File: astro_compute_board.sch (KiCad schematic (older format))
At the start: 76 parts, among them J1 SWD, J2 Conn_01x04, J3 Conn_01x04, J4 Heater01, J5 GPIO_CONNECTOR, J6 USB_B_Micro, J7 Heater01, J8 RaspberryHeader, Q1 QM6015D, Q2 IRF540S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

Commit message: Board almost done. Major simplifications ahead
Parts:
- added H1, H2, H3, H4: MountingHole_Pad, MountingHole:MountingHole_3.2mm_M3_Pad_Via, symbol Mechanical:MountingHole_Pad
- added J10: ADC_IO, Connector_Molex:Molex_PicoBlade_53048-0510_1x05_P1.25mm_Horizontal, symbol Connector_Generic:Conn_01x05
- C1, C2: footprint (none) -> Capacitor_SMD:C_0603_1608Metric
- C10, C11, C12, C3, C4, C5, C6, C7, C8, C9: footprint (none) -> Capacitor_SMD:C_0402_1005Metric
- C13, C14, C15, C16, C17, C18: footprint (none) -> Capacitor_SMD:C_1206_3216Metric
- C19, C20, C21, C22, C23, C24: renamed from C?; footprint (none) -> Capacitor_SMD:C_1206_3216Metric
- D1: footprint (none) -> LED_SMD:LED_0603_1608Metric
- F1: footprint (none) -> Fuse:Fuse_1206_3216Metric
- FB1: footprint (none) -> Inductor_SMD:L_0805_2012Metric
- GPIO1: renamed from J5; footprint (none) -> Connector_PinHeader_1.27mm:PinHeader_2x05_P1.27mm_Vertical_SMD
- J1: footprint (none) -> Connector_PinHeader_1.27mm:PinHeader_2x05_P1.27mm_Vertical_SMD
- J2: value Conn_01x04 -> I2C1; footprint (none) -> Connector_Molex:Molex_PicoBlade_53048-0410_1x04_P1.25mm_Horizontal
- J6: footprint (none) -> Connector_USB:USB_Micro-AB_Molex_47590-0001
- J8: footprint (none) -> Connector_PinHeader_2.54mm:PinHeader_2x20_P2.54mm_Vertical
- J9: renamed from J?; value Heater01 -> VINPUT
- L1: footprint (none) -> Inductor_SMD:L_0402_1005Metric
- L2: footprint (none) -> Inductor_SMD:L_Sunlord_MWSA0518_5.4x5.2mm
- L3: renamed from L?; footprint (none) -> Inductor_SMD:L_Sunlord_MWSA0518_5.4x5.2mm
- R1, R12, R13, R14, R15, R16, R17, R2: footprint (none) -> Resistor_SMD:R_0402_1005Metric
- R10, R11, R18, R19, R3, R6, R7, R8, R9: footprint (none) -> Resistor_SMD:R_0603_1608Metric
- R20, R21: renamed from R?; footprint (none) -> Resistor_SMD:R_0805_2012Metric
- R22, R23, R24, R25: renamed from R?; footprint (none) -> Resistor_SMD:R_0603_1608Metric
- R4, R5: footprint (none) -> Resistor_SMD:R_0805_2012Metric
- SW1: footprint (none) -> Button_Switch_SMD:SW_SPDT_PCM12
- U2: footprint (none) -> Package_SO:SOIC-8-1EP_3.9x4.9mm_P1.27mm_EP2.29x3mm
- U4: renamed from U?; footprint (none) -> Package_SO:SOIC-8-1EP_3.9x4.9mm_P1.27mm_EP2.29x3mm
- USART1: renamed from J3; footprint (none) -> Connector_Molex:Molex_PicoBlade_53048-0410_1x04_P1.25mm_Horizontal
- Y1: footprint (none) -> Crystal:Crystal_SMD_3225-4Pin_3.2x2.5mm
- gave numbers to parts that had none: 1
- renumbered J4 to Heater1, J7 to Heater2
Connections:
- wire segments 254 -> 263
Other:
- moved on the sheet: C19, C20, C21, C22, C23, C24, J9, L3, R22, R23, R24, R25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

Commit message: JLCPCB Ready (but costly)
Contains many extender parts that make PCB expensive.
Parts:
- removed C21: Open, Capacitor_SMD:C_1206_3216Metric, symbol Device:C_Small
- removed C22: 0.1u, Capacitor_SMD:C_1206_3216Metric, symbol Device:C_Small
- removed C23: 2.2nF, Capacitor_SMD:C_1206_3216Metric, symbol Device:C_Small
- removed C24: 22uF, Capacitor_SMD:C_1206_3216Metric, symbol Device:C_Small
- removed J2: I2C1, Connector_Molex:Molex_PicoBlade_53048-0410_1x04_P1.25mm_Horizontal, symbol Connector_Generic:Conn_01x04
- removed L3: 6.8uH, Inductor_SMD:L_Sunlord_MWSA0518_5.4x5.2mm, symbol Device:L_Small
- removed R25: 24k, Resistor_SMD:R_0603_1608Metric, symbol Device:R_Small
- removed TP1, TP2: TestPoint, TestPoint:TestPoint_Pad_D2.0mm, symbol Connector:TestPoint
- removed U4: RT7257BHZSP, Package_SO:SOIC-8-1EP_3.9x4.9mm_P1.27mm_EP2.29x3mm, symbol project_custom_symbols:RT7257BHZSP
- added D2: B5817W-5819W, Diode_SMD:D_SOD-123, symbol Device:D_Schottky_Small
- added D3, D4: RED, LED_SMD:LED_0603_1608Metric, symbol Device:LED_Small
- added D5: Green, LED_SMD:LED_0603_1608Metric, symbol Device:LED_Small
- added U4: LM1117-3.3, Package_TO_SOT_SMD:SOT-223, symbol Regulator_Linear:LM1117-3.3
- C1, C2: LCSC Part # (none) -> C23630
- C10: LCSC Part # (none) -> C15195
- C11, C12: LCSC Part # (none) -> C1547
- C13, C19, C20: LCSC Part # (none) -> C13585
- C14, C16: LCSC Part # (none) -> C24497
- C15: value Open -> 22uF; LCSC Part # (none) -> C5672
- C17: LCSC Part # (none) -> C35220
- C18: LCSC Part # (none) -> C5672
- C3: value 4uF -> 4.7uF; LCSC Part # (none) -> C23733
- C4, C5, C6, C7, C8: LCSC Part # (none) -> C1525
- C9: LCSC Part # (none) -> C52923
- D1: value LED_Small -> BLUE; LCSC Part # (none) -> C72041
- F1: LCSC Part # (none) -> C315895
- FB1: LCSC Part # (none) -> C1017
- L1: LCSC Part # (none) -> C26443
- L2: LCSC Part # (none) -> C408348
- Q1: LCSC Part # (none) -> C238708
- Q2, Q3: LCSC Part # (none) -> C725068
- R1: LCSC Part # (none) -> C25744
- R10, R18: LCSC Part # (none) -> C21190
- R11, R19: LCSC Part # (none) -> C22961
- R12, R13, R14, R15, R16, R17: LCSC Part # (none) -> C25092
- R2: LCSC Part # (none) -> C25118
- R20, R21, R4, R5: LCSC Part # (none) -> C17520
- R22: value 100k -> 1k; LCSC Part # (none) -> C21190
- R23: value 22k -> 1k; LCSC Part # (none) -> C21190
- R24: value 75k -> 1k; LCSC Part # (none) -> C21190
- R3: value 10k -> 2k; LCSC Part # (none) -> C22975
- R6: LCSC Part # (none) -> C25803
- R7: value 22k -> 33k; LCSC Part # (none) -> C4216
- R8: value 75k -> 62k; LCSC Part # (none) -> C23221
- R9: value 24k -> 11.8k; LCSC Part # (none) -> C22861
- U1: LCSC Part # (none) -> C15742
- U2: LCSC Part # (none) -> C27998
- U3: LCSC Part # (none) -> C7519
- U5: LCSC Part # (none) -> C94847
- Y1: LCSC Part # (none) -> C13738
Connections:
- net labels removed: PWM_A1, PWM_B1
- wire segments 263 -> 238
- no-connect marks 50 -> 53
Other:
- moved on the sheet: C13, C14, C16, C17, C18, H1, H2, H3, H4, Heater1, Heater2, J9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

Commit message: Rev2 - Out of Stock componets update (JLCPCB)
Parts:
- added R25: 800, Resistor_SMD:R_0603_1608Metric, symbol Device:R_Small
- C15, C18: footprint Capacitor_SMD:C_1206_3216Metric -> Capacitor_SMD:C_0805_2012Metric; LCSC Part # C5672 -> C45783
- C17: footprint Capacitor_SMD:C_1206_3216Metric -> Capacitor_SMD:C_0805_2012Metric; LCSC Part # C35220 -> C28260
- D2: LCSC Part # C84032 -> C8598
- F1: LCSC Part # C315895 -> (none)
- J6: footprint Connector_USB:USB_Micro-AB_Molex_47590-0001 -> Connector_USB:USB_Micro-B_Molex-105017-0001; LCSC Part # (none) -> C404969
- Q2, Q3: symbol IRF540:IRF540 -> astro_compute_board-rescue:IRF540-IRF540
- R9: value 11.8k -> 11k; LCSC Part # C22861 -> C25950
- SW1: LCSC Part # (none) -> C431541
- U1: value STM32F405RGTx -> STM32F103R8T6; LCSC Part # C15742 -> C46034
- U2: LCSC Part # C27998 -> C130799
- U5: LCSC Part # C94847 -> C129490
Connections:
- net +3V3: no longer J8.1 (Pin_1), J8.17 (Pin_17)
- net GND: now also R25.1; no longer R9.1
- new net: R25.2, R9.1
- no-connect marks 53 -> 55
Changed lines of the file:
@@
 encoding utf-8
 Sheet 1 1
-Title "Astro Compute Raspberry Pi Zero W + STM32"
-Date "2020-11-18"
-Rev "1"
+Title "Astro Compute Raspberry Pi + STM32"
+Date "2021-04-11"
+Rev "2"
 Comp ""
 Comment1 ""
@@
 P 2050 5400
 F 0 "U1" H 1500 3650 50  0000 C CNN
-F 1 "STM32F405RGTx" H 2500 3650 50  0000 C CNN
+F 1 "STM32F103R8T6" H 2500 3650 50  0000 C CNN
 F 2 "Package_QFP:LQFP-64_10x10mm_P0.5mm" H 1450 3700 50  0001 R CNN
-F 3 "http://www.st.com/st-web-ui/static/active/en/resource/technical/document/datasheet/DM00037051.pdf" H 2050 5400 50  0001 C CNN
-F 4 "C15742" H 2050 5400 50  0001 C CNN "LCSC Part #"
+F 3 "https://datasheet.lcsc.com/szlcsc/STMicroelectronics-STM32F103R8T6_C46034.pdf" H 2050 5400 50  0001 C CNN
+F 4 "C46034" H 2050 5400 50  0001 C CNN "LCSC Part #"
 	1    2050 5400
 	1    0    0    -1
@@
 F 1 "SW_SPDT" H 4400 3794 50  0000 C CNN
 F 2 "Button_Switch_SMD:SW_SPDT_PCM12" H 4400 3600 50  0001 C CNN
-F 3 "~" H 4400 3600 50  0001 C CNN
+F 3 "https://datasheet.lcsc.com/szlcsc/1912111437_SHOU-HAN-MSK12C02-HB_C431541.pdf" H 4400 3600 50  0001 C CNN
+F 4 "C431541" H 4400 3600 50  0001 C CNN "LCSC Part #"
 	1    4400 3600
 	1    0    0    -1
@@
 F 2 "Package_SO:SOIC-8-1EP_3.9x4.9mm_P1.27mm_EP2.29x3mm" H 3950 1150 50  0001 C CNN
 F 3 "" H 3950 1150 50  0001 C CNN
-F 4 "C27998" H 3950 1150 50  0001 C CNN "LCSC Part #"
+F 4 "C130799" H 3950 1150 50  0001 C CNN "LCSC Part #"
 	1    3950 1150
 	1    0    0    -1
@@
 F 1 "3A" V 750 900 50  0000 L CNN
 F 2 "Fuse:Fuse_1206_3216Metric" H 700 1050 50  0001 C CNN
-F 3 "~" H 700 1050 50  0001 C CNN
-F 4 "C315895" H 700 1050 50  0001 C CNN "LCSC Part #"
+F 3 "C315895 Do not SMT" H 700 1050 50  0001 C CNN
+F 4 "" H 700 1050 50  0001 C CNN "LCSC Part #"
 	1    700  1050
 	0    1    1    0
@@
 P 5150 1500
 F 0 "R9" H 5091 1454 50  0000 R CNN
-F 1 "11.8k" H 5091 1545 50  0000 R CNN
+F 1 "11k" H 5091 1545 50  0000 R CNN
 F 2 "Resistor_SMD:R_0603_1608Metric" H 5150 1500 50  0001 C CNN
 F 3 "~" H 5150 1500 50  0001 C CNN
-F 4 "C22861" H 5150 1500 50  0001 C CNN "LCSC Part #"
+F 4 "C25950" H 5150 1500 50  0001 C CNN "LCSC Part #"
 	1    5150 1500
 	-1   0    0    1
@@
 F 0 "C18" H 5600 1450 50  0000 L CNN
 F 1 "22uF" H 5550 1300 50  0000 L CNN
-F 2 "Capacitor_SMD:C_1206_3216Metric" H 5750 1400 50  0001 C CNN
+F 2 "Capacitor_SMD:C_0805_2012Metric" H 5750 1400 50  0001 C CNN
 F 3 "~" H 5750 1400 50  0001 C CNN
-F 4 "C5672" H 5750 1400 50  0001 C CNN "LCSC Part #"
+F 4 "C45783" H 5750 1400 50  0001 C CNN "LCSC Part #"
 	1    5750 1400
 	1    0    0    -1
@@
 L power:GND #PWR021
 U 1 1 5FC1E445
-P 5150 1700
-F 0 "#PWR021" H 5150 1450 50  0001 C CNN
-F 1 "GND" H 5155 1527 50  0000 C CNN
-F 2 "" H 5150 1700 50  0001 C CNN
-F 3 "" H 5150 1700 50  0001 C CNN
-	1    5150 1700
+P 5150 1950
+F 0 "#PWR021" H 5150 1700 50  0001 C CNN
+F 1 "GND" H 5155 1777 50  0000 C CNN
+F 2 "" H 5150 1950 50  0001 C CNN
+F 3 "" H 5150 1950 50  0001 C CNN
+	1    5150 1950
 	1    0    0    -1
 $EndComp
@@
 F 0 "C17" H 4600 1650 50  0000 L CNN
 F 1 "2.2nF" H 4550 1450 50  0000 L CNN
-F 2 "Capacitor_SMD:C_1206_3216Metric" H 4750 1550 50  0001 C CNN
+F 2 "Capacitor_SMD:C_0805_2012Metric" H 4750 1550 50  0001 C CNN
 F 3 "~" H 4750 1550 50  0001 C CNN
-F 4 "C35220" H 4750 1550 50  0001 C CNN "LCSC Part #"
+F 4 "C28260" H 4750 1550 50  0001 C CNN "LCSC Part #"
 	1    4750 1550
 	-1   0    0    1
@@
 Connection ~ 10900 4550
 $Comp
-L power:+3.3V #PWR038
-U 1 1 5FDCF1C5
-P 9600 2850
-F 0 "#PWR038" H 9600 2700 50  0001 C CNN
-F 1 "+3.3V" H 9615 3023 50  0000 C CNN
-F 2 "" H 9600 2850 50  0001 C CNN
-F 3 "" H 9600 2850 50  0001 C CNN
-	1    9600 2850
-	1    0    0    -1
-$EndComp
-Wire Wire Line
-	9600 2850 9600 2950
-Wire Wire Line
-	9600 2950 10000 2950
-$Comp
-L power:+3.3V #PWR042
-U 1 1 5FDD723B
-P 9800 3750
-F 0 "#PWR042" H 9800 3600 50  0001 C CNN
-F 1 "+3.3V" H 9815 3923 50  0000 C CNN
-F 2 "" H 9800 3750 50  0001 C CNN
-F 3 "" H 9800 3750 50  0001 C CNN
-	1    9800 3750
-	1    0    0    -1
-$EndComp
-Wire Wire Line
-	9800 3750 10000 3750
-$Comp
 L power:+5V #PWR043
 U 1 1 5FDE0707
@@
 F 0 "J6" H 7107 6267 50  0000 C CNN
 F 1 "USB_B_Micro" H 7107 6176 50  0000 C CNN
-F 2 "Connector_USB:USB_Micro-AB_Molex_47590-0001" H 7200 5750 50  0001 C CNN
-F 3 "~" H 7200 5750 50  0001 C CNN
+F 2 "Connector_USB:USB_Micro-B_Molex-105017-0001" H 7200 5750 50  0001 C CNN
+F 3 "https://datasheet.lcsc.com/szlcsc/1912111437_SHOU-HAN-MicroXNJ_C404969.pdf" H 7200 5750 50  0001 C CNN
+F 4 "C404969" H 7050 5800 50  0001 C CNN "LCSC Part #"
 	1    7050 5800
 	1    0    0    -1
@@
 GPIO_07
 $Comp
-L IRF540:IRF540 Q3
+L astro_compute_board-rescue:IRF540-IRF540 Q3
 U 1 1 5FE9B193
 P 8350 3250
@@
 	6450 2750 6450 2850
 $Comp
-L IRF540:IRF540 Q2
+L astro_compute_board-rescue:IRF540-IRF540 Q2
 U 1 1 5FF1D605
 P 6350 3250
@@
 F 2 "Package_SO:MSOP-8_3x3mm_P0.65mm" H 8500 4600 50  0001 C CNN
 F 3 "http://ww1.microchip.com/downloads/en/DeviceDoc/22203b.pdf" H 8250 5050 50  0001 C CNN
-F 4 "C94847" H 8500 4600 50  0001 C CNN "LCSC Part #"
+F 4 "C129490" H 8500 4600 50  0001 C CNN "LCSC Part #"
 	1    8500 4600
 	1    0    0    -1
@@
 F 2 "Diode_SMD:D_SOD-123" V 1350 1000 50  0001 C CNN
 F 3 "~" V 1350 1000 50  0001 C CNN
-F 4 "C84032" H 1350 1000 50  0001 C CNN "LCSC Part #"
+F 4 "C8598" H 1350 1000 50  0001 C CNN "LCSC Part #"
 	1    1350 1000
 	0    -1   -1   0
@@
 F 0 "C15" H 5900 1450 50  0000 L CNN
 F 1 "22uF" H 5850 1300 50  0000 L CNN
-F 2 "Capacitor_SMD:C_1206_3216Metric" H 6050 1400 50  0001 C CNN
+F 2 "Capacitor_SMD:C_0805_2012Metric" H 6050 1400 50  0001 C CNN
 F 3 "~" H 6050 1400 50  0001 C CNN
-F 4 "C5672" H 6050 1400 50  0001 C CNN "LCSC Part #"
+F 4 "C45783" H 6050 1400 50  0001 C CNN "LCSC Part #"
 	1    6050 1400
 	1    0    0    -1
@@
 LED_STATUS
 NoConn ~ 1350 7000
+$Comp
+L Device:R_Small R25
+U 1 1 607D8237
+P 5150 1800
+F 0 "R25" H 5091 1754 50  0000 R CNN
+F 1 "800" H 5091 1845 50  0000 R CNN
+F 2 "Resistor_SMD:R_0603_1608Metric" H 5150 1800 50  0001 C CNN
+F 3 "~" H 5150 1800 50  0001 C CNN
+F 4 "C23228" H 5150 1800 50  0001 C CNN "LCSC Part #"
+	1    5150 1800
+	-1   0    0    1
+$EndComp
+Wire Wire Line
+	5150 1900 5150 1950
+NoConn ~ 10000 2950
+NoConn ~ 10000 3750
 $EndSCHEMATC

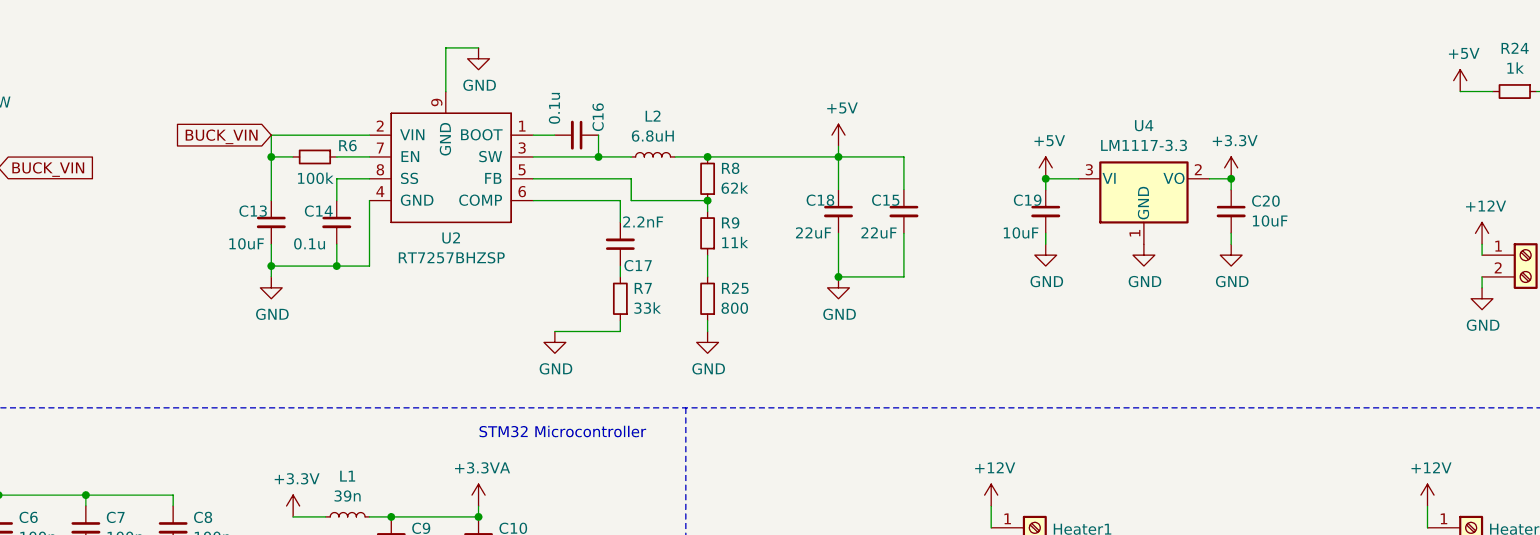
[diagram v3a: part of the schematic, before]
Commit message: Rev2.1 - Redesigned using Bulk Coverter and TH componets for easy testing
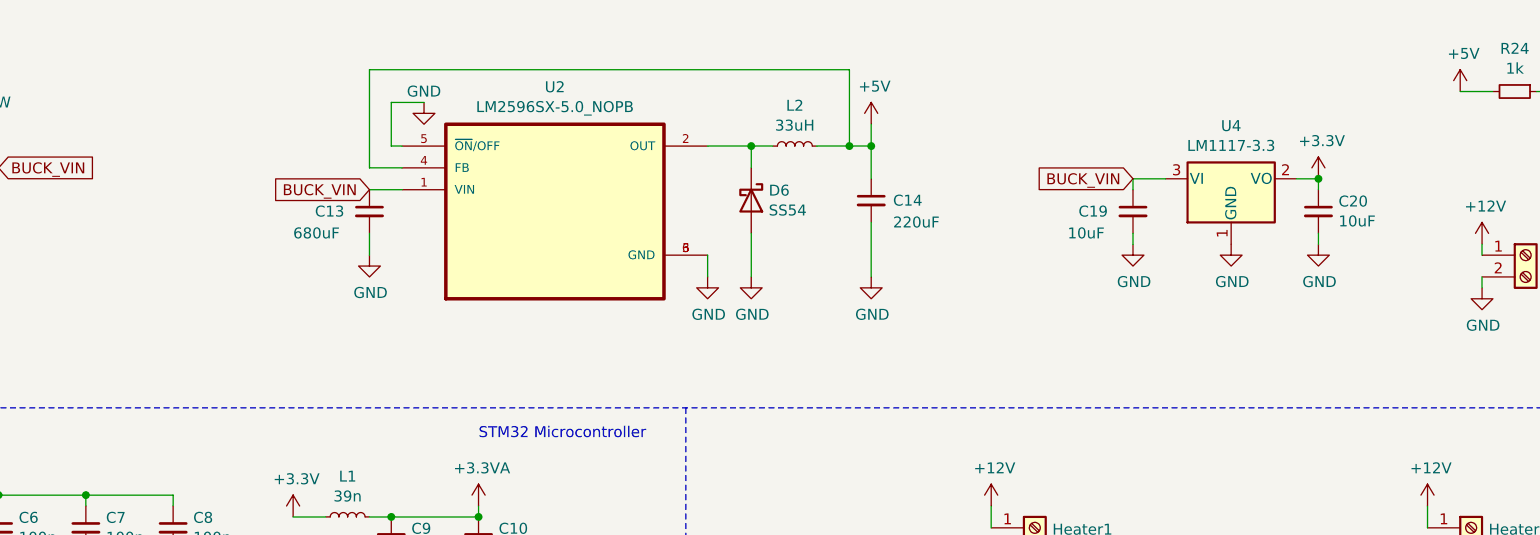
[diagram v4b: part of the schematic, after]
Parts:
- removed C15, C18: 22uF, Capacitor_SMD:C_0805_2012Metric, symbol Device:C_Small
- removed C16: 0.1u, Capacitor_SMD:C_1206_3216Metric, symbol Device:C_Small
- removed C17: 2.2nF, Capacitor_SMD:C_0805_2012Metric, symbol Device:C_Small
- removed R25: 800, Resistor_SMD:R_0603_1608Metric, symbol Device:R_Small
- removed R6: 100k, Resistor_SMD:R_0603_1608Metric, symbol Device:R_Small
- removed R7: 33k, Resistor_SMD:R_0603_1608Metric, symbol Device:R_Small
- removed R8: 62k, Resistor_SMD:R_0603_1608Metric, symbol Device:R_Small
- removed R9: 11k, Resistor_SMD:R_0603_1608Metric, symbol Device:R_Small
- removed U2: RT7257BHZSP, Package_SO:SOIC-8-1EP_3.9x4.9mm_P1.27mm_EP2.29x3mm, symbol project_custom_symbols:RT7257BHZSP
- added D6: SS54, Diode_SMD:D_SMA, symbol Diode:1N5822
- added U2: LM2596SX-5.0_NOPB, lib:NOPB, symbol LM2596:LM2596SX-5.0_NOPB
- C13: value 10uF -> 680uF; footprint Capacitor_SMD:C_1206_3216Metric -> Capacitor_THT:CP_Radial_D8.0mm_P3.50mm
- C14: value 0.1u -> 220uF; footprint Capacitor_SMD:C_1206_3216Metric -> Capacitor_THT:CP_Radial_D6.3mm_P2.50mm; LCSC Part # C24497 -> C13585
- L2: value 6.8uH -> 33uH; footprint Inductor_SMD:L_Sunlord_MWSA0518_5.4x5.2mm -> Inductor_THT:L_Radial_D7.5mm_P3.50mm_Fastron_07P; LCSC Part # C408348 -> (none)
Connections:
- net +5V: now also C14.1, U2.4 (FB); no longer C19.1, U4.3 (VI)
- net BUCK_VIN: now also C19.1, U4.3 (VI), U2.1 (VIN)
- net GND: now also D6.2 (A), U2.3 (GND), U2.5 (~ON~/OFF), U2.6 (GND)
- net at L2.1: now also D6.1 (K), U2.2 (OUT)
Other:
- moved on the sheet: C19, C20, U4
